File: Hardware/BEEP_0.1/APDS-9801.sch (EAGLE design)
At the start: 8 parts, among them IC1 APDS-9801

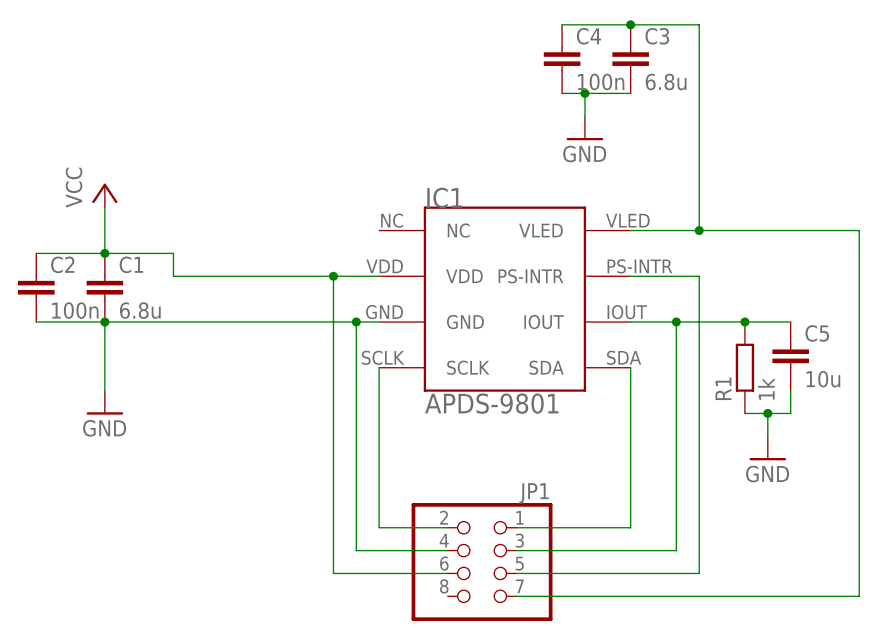
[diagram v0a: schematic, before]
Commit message: Add branding ;) enhance PCBs finish Easy RGB Board add Texas Instruments libray from Element 14 add dxf import ulp for eagle add Script for easy eagle export to pdf for etching minor cleanup
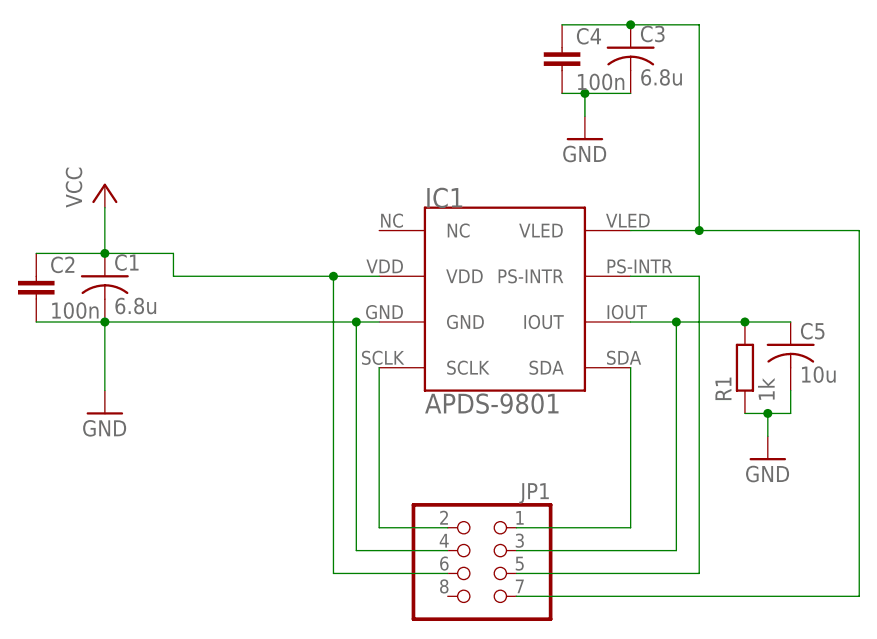
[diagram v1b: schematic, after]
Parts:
- C1, C3, C5: device rcl:C-EUC0805 -> rcl:C-US025-024X044
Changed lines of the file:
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@@
 <parts>
 <part name="IC1" library="BEEP" deviceset="APDS-9801" device=""/>
-<part name="C1" library="rcl" deviceset="C-EU" device="C0805" value="6.8u"/>
+<part name="C1" library="rcl" deviceset="C-US" device="025-024X044" value="6.8u"/>
 <part name="C4" library="rcl" deviceset="C-EU" device="C0805" value="100n"/>
-<part name="C5" library="rcl" deviceset="C-EU" device="C0805" value="10u"/>
+<part name="C5" library="rcl" deviceset="C-US" device="025-024X044" value="10u"/>
 <part name="R1" library="rcl" deviceset="R-EU_" device="M0805" value="1k"/>
 <part name="C2" library="rcl" deviceset="C-EU" device="C0805" value="100n"/>
-<part name="C3" library="rcl" deviceset="C-EU" device="C0805" value="6.8u"/>
+<part name="C3" library="rcl" deviceset="C-US" device="025-024X044" value="6.8u"/>
 <part name="P+1" library="supply1" deviceset="VCC" device=""/>
 <part name="GND1" library="supply1" deviceset="GND" device=""/>
